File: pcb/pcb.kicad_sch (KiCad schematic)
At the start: 36 parts, among them J1 Conn_01x04, J2 Conn_01x04, J3 UPDI, SW1 MX Grey w/ LED, SW2 MX Grey w/ LED, SW3 1241.1100.7095, U1 Display Driver, U2 Display Driver, U3 MCU, U4 OR, 2 Channels, U5 Voltage Regulator, Y1 32kHz

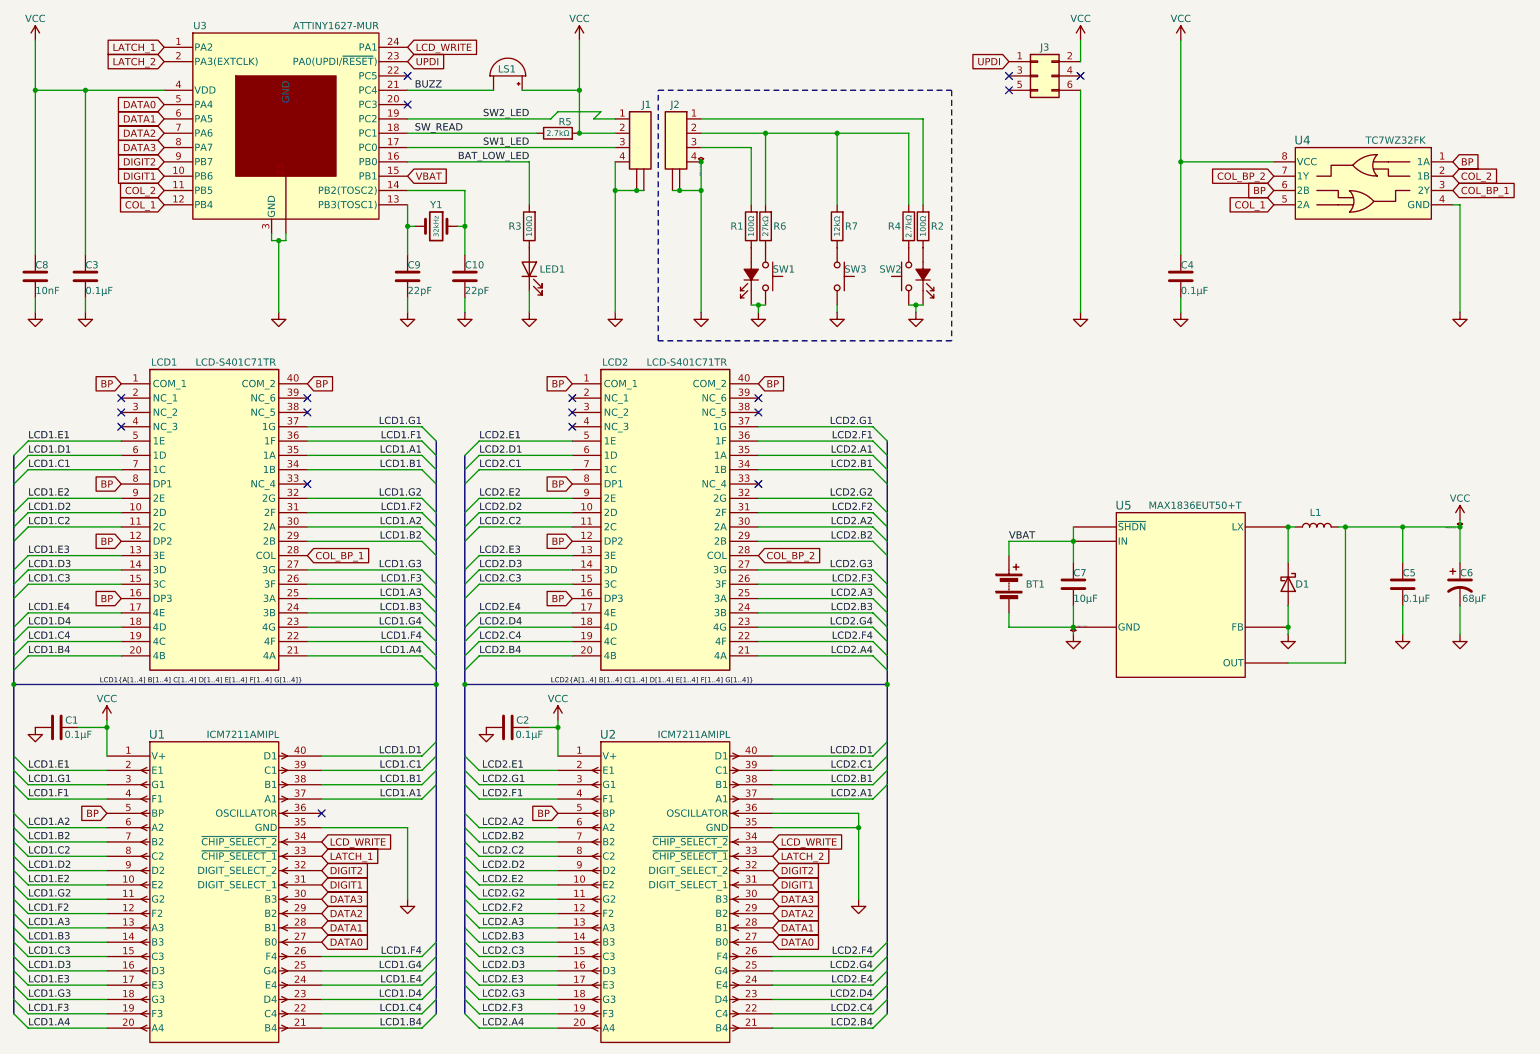
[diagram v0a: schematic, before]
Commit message: Finalize initial design
Signed-off-by: Michael Darr <mdarr@tesla.com>
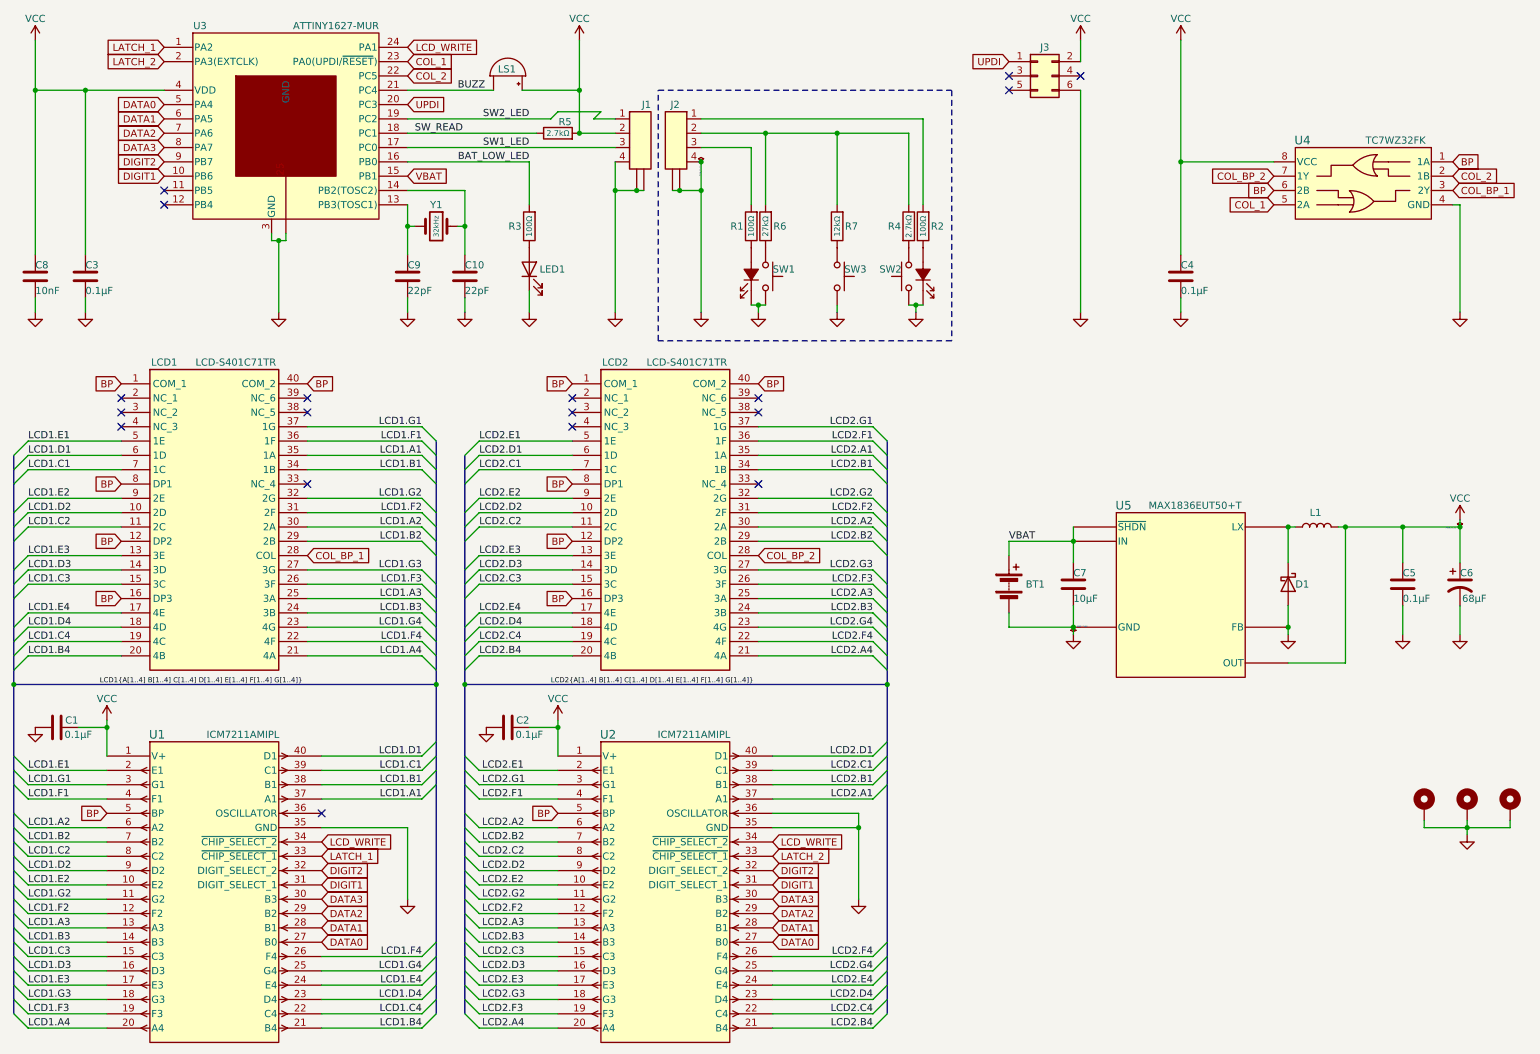
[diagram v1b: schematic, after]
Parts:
- added H1, H2, H3: MountingHole_Pad, MountingHole:MountingHole_3.5mm_Pad_TopBottom, symbol Mechanical:MountingHole_Pad
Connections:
- net COL_1: now also U3.23 (PA0(UPDI/~{RESET})); no longer U3.12 (PB4)
- net COL_2: now also U3.22 (PC5); no longer U3.11 (PB5)
- net GND: now also H1.1, H2.1, H3.1
- net UPDI: now also U3.20 (PC3); no longer U3.23 (PA0(UPDI/~{RESET}))

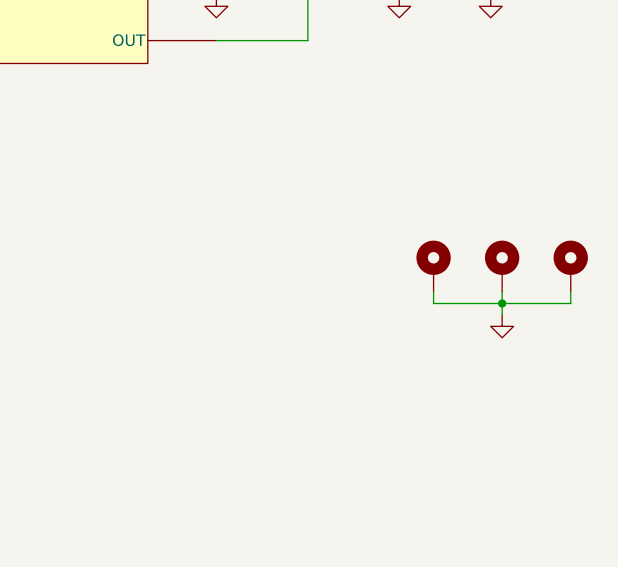
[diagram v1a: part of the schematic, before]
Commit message: Add extensive mounting holes
Signed-off-by: Michael Darr <mdarr@tesla.com>
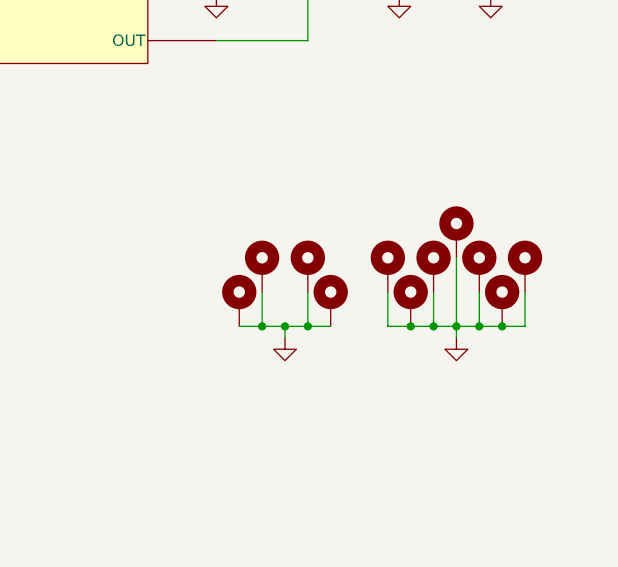
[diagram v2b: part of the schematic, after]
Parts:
- added H10, H11, H4, H5, H6, H7, H8, H9: MountingHole_Pad, MountingHole:MountingHole_3.5mm_Pad_TopBottom, symbol Mechanical:MountingHole_Pad
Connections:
- net GND: now also H4.1, H5.1, H6.1, H7.1
- net GND1: now also H10.1, H11.1, H8.1, H9.1

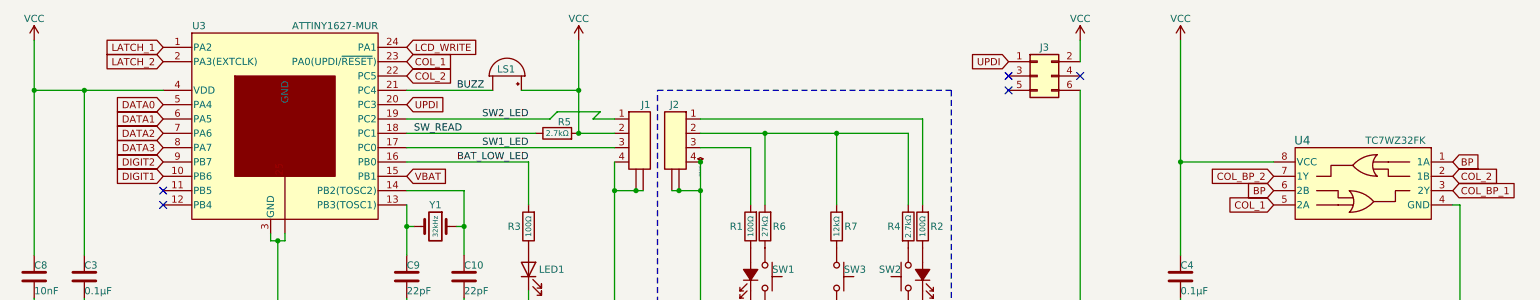
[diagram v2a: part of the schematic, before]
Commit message: Fix many issues
Signed-off-by: Michael Darr <mdarr@tesla.com>
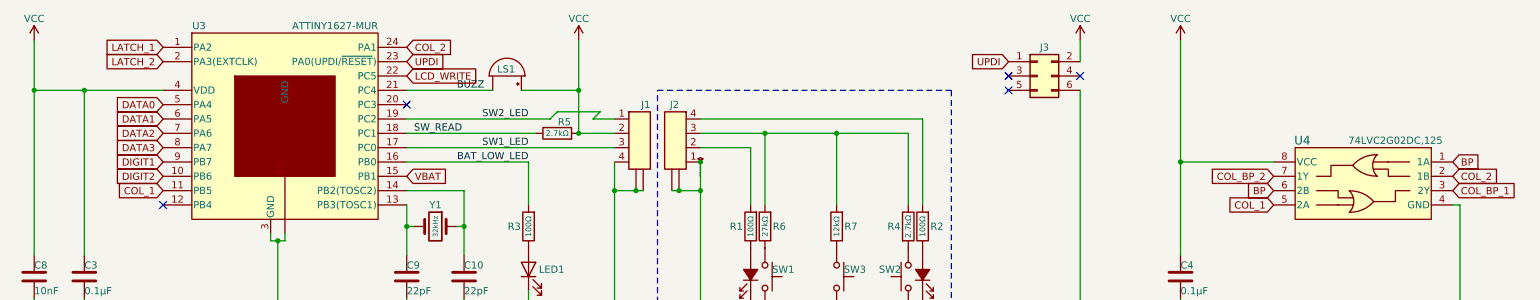
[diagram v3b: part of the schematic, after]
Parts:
- U4: value OR, 2 Channels -> NOR, 2 Channels; PN TC7WZ32FK -> 74LVC2G02DC,125
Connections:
- net COL_1: now also U3.11 (PB5); no longer U3.23 (PA0(UPDI/~{RESET}))
- net COL_2: now also U3.24 (PA1); no longer U3.22 (PC5)
- net DIGIT1: now also U3.9 (PB7); no longer U3.10 (PB6)
- net DIGIT2: now also U3.10 (PB6); no longer U3.9 (PB7)
- net GND1: now also J2.1; no longer J2.4
- net LCD_WRITE: now also U3.22 (PC5); no longer U3.24 (PA1)
- net UPDI: now also U3.23 (PA0(UPDI/~{RESET})); no longer U3.20 (PC3)
- net at R4.1, R6.2, R7.2: now also J2.3; no longer J2.2
- net at R2.2: now also J2.4; no longer J2.1
- net at R1.2: now also J2.2; no longer J2.3

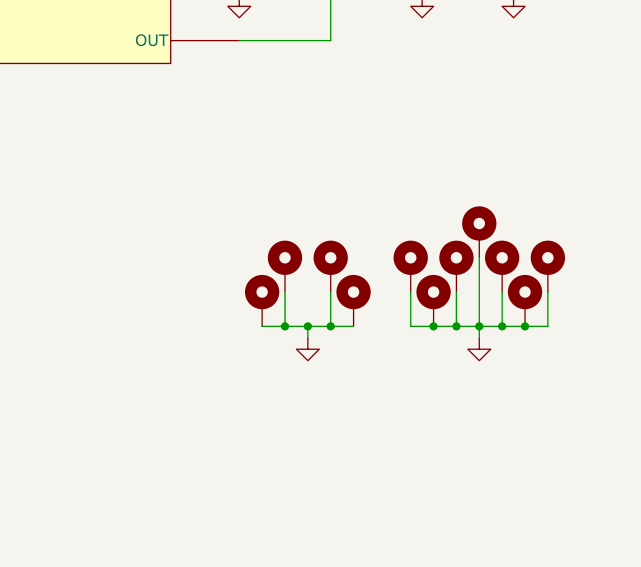
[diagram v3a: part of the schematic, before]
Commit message: Fix pcb issues
Signed-off-by: Michael Darr <mdarr@tesla.com>
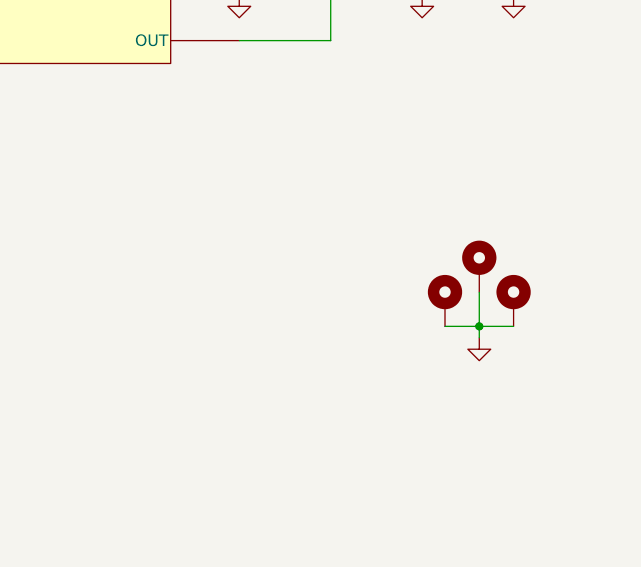
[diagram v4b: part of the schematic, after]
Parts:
- removed H10, H11, H4, H5, H6, H7, H8, H9: MountingHole_Pad, MountingHole:MountingHole_3.5mm_Pad_TopBottom, symbol Mechanical:MountingHole_Pad

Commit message: Fine adjustments
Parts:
- R1, R2: value 100Ω -> 1.2kΩ; PN RC2012J101CS -> (none)
- SW1, SW2: Notes LED PN: INL-3AG30 [datasheet](https://www.inolux-corp.com/d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 -> LED PN: XZCDGK53W-8VF
